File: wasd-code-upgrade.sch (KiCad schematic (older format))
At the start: 24 parts, among them J101 Conn_ARM_JTAG_SWD_10, J102 TC2030, J103 OLED, Q101 ZXTN08400BFF, Q102 ZXTP25020CFFTA, U101 STM32L422CBTx, U102 MIC5205-3.3YM5, U103 TC74VHC238F

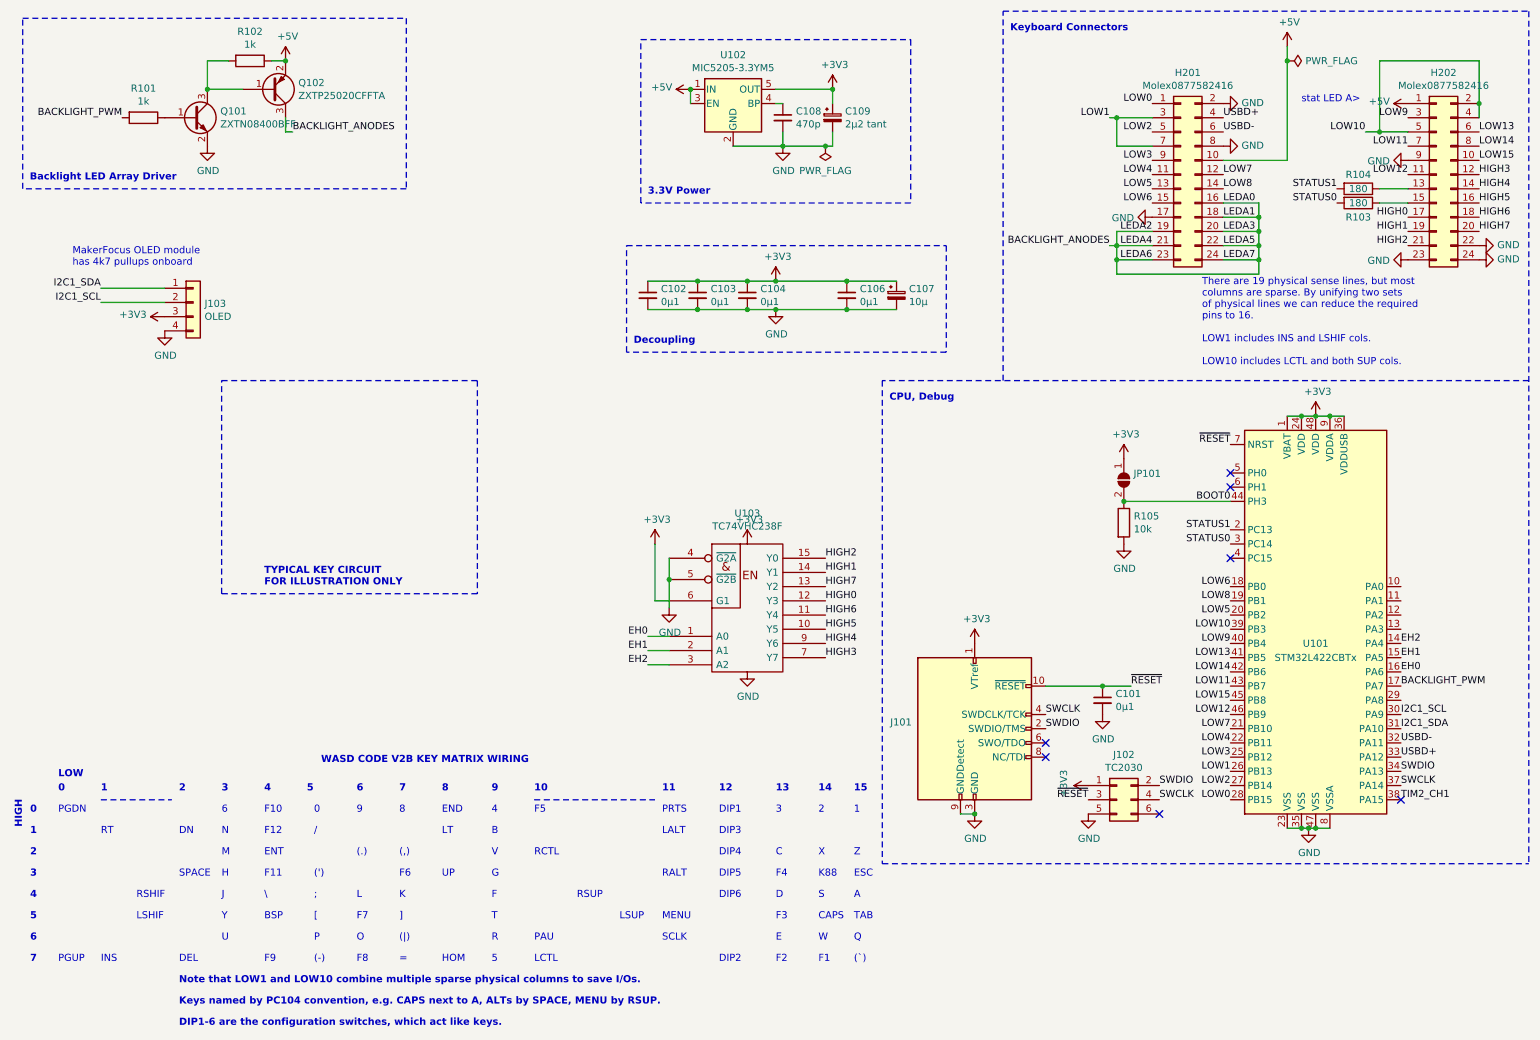
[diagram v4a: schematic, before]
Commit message: wasd-code-upgrade: tidy schematic
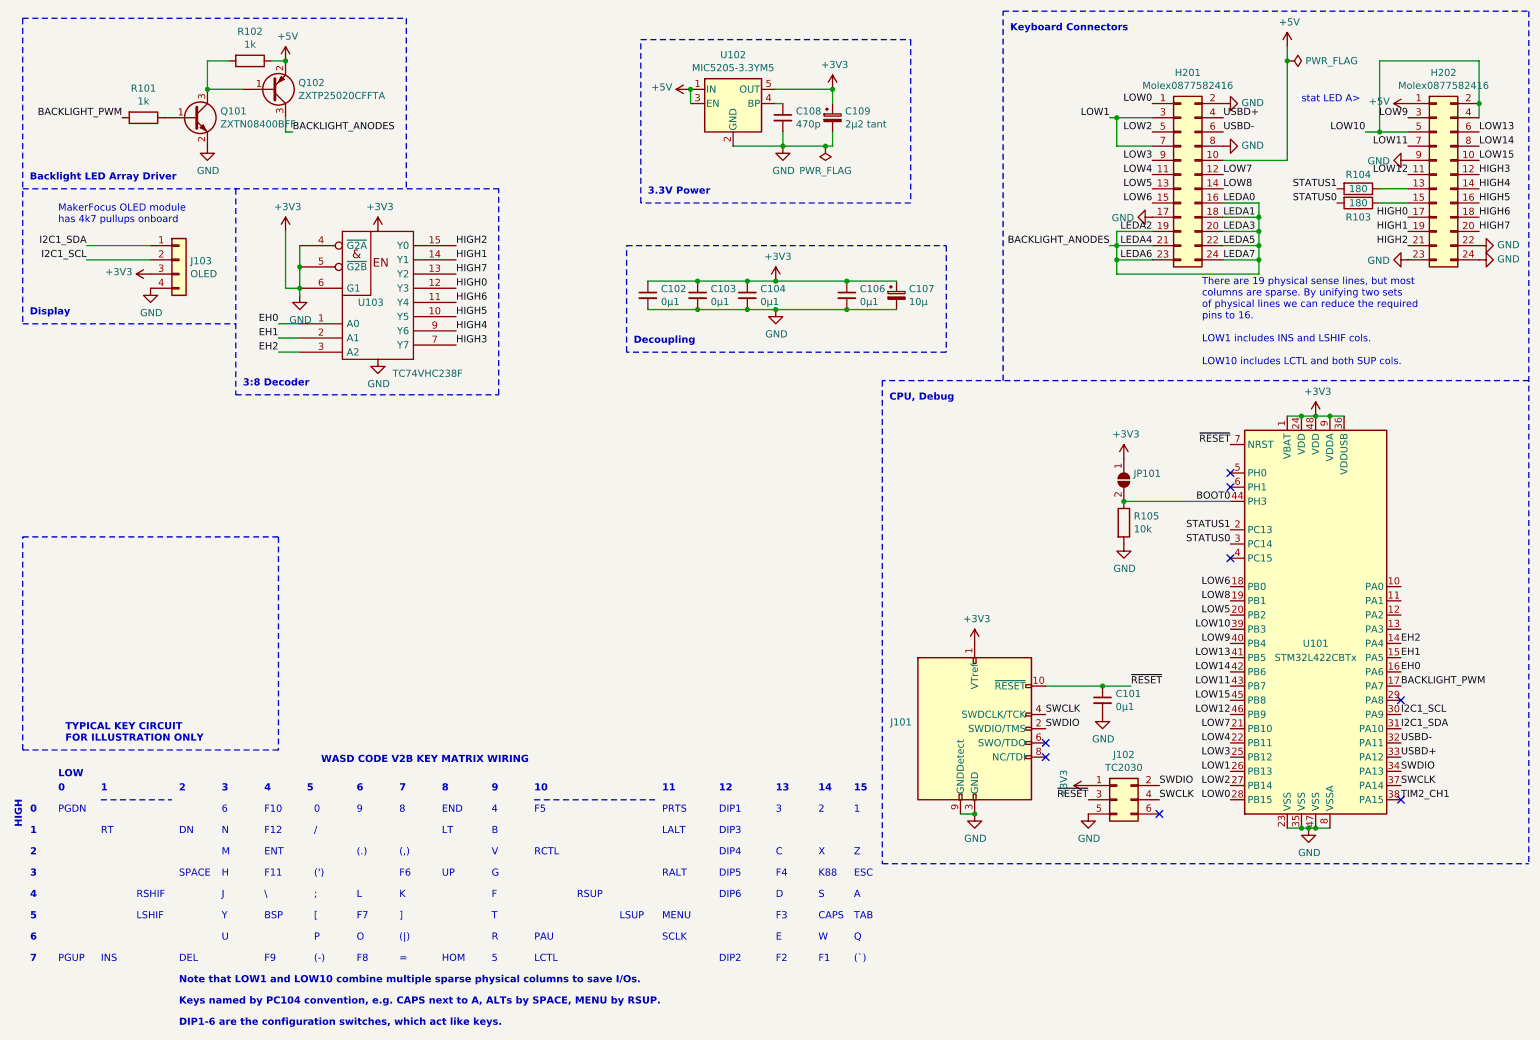
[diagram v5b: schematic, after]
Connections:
- net GND is gone; now on net +3V3: C101.2, C102.2, C103.2, C104.2, C106.2, C107.2, C108.2, C109.2, H201.17 (Pin_17), H201.2 (Pin_2), H201.8 (Pin_8), H202.22 (Pin_22), H202.23 (Pin_23), H202.24 (Pin_24), H202.9 (Pin_9), J101.3 (GND), J101.5 (GND), J101.9 (GNDDetect), J102.5 (Pin_5), J103.4 (Pin_4), Q101.2 (E), R105.2, U101.23 (VSS), U101.35 (VSS), U101.47 (VSS), U101.8 (VSSA), U102.2 (GND), U103.4 (~G2A), U103.5 (~G2B), U103.8 (GND)
- no-connect marks 7 -> 8
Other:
- note added: "3:8 Decoder"
- note added: "Display"
- moved on the sheet: J103, U103
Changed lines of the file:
@@
 Note that LOW1 and LOW10 combine multiple sparse physical columns to save I/Os.
 $Bitmap
-Pos 2900 3750
+Pos 1500 4850
 Scale 1.000000
 Data
@@
 EndData
 $EndBitmap
-Text Notes 2300 4550 0    50   ~ 10
+Text Notes 900  5650 0    50   ~ 10
 TYPICAL KEY CIRCUIT\nFOR ILLUSTRATION ONLY
 Wire Notes Line
-	2000 3100 3800 3100
-Wire Notes Line
-	3800 3100 3800 4600
-Wire Notes Line
-	3800 4600 2000 4600
-Wire Notes Line
-	2000 4600 2000 3100
+	600  4200 2400 4200
+Wire Notes Line
+	2400 4200 2400 5700
+Wire Notes Line
+	2400 5700 600  5700
+Wire Notes Line
+	600  5700 600  4200
 Text Notes 2700 5800 0    50   ~ 10
 WASD CODE V2B KEY MATRIX WIRING
@@
 Wire Notes Line
 	3300 550  3300 1750
-Wire Notes Line
-	3300 1750 600  1750
-Wire Notes Line
-	600  1750 600  550
 Wire Notes Line
 	600  550  3300 550
@@
 L power:+3V3 #PWR0126
 U 1 1 5F3B29C9
-P 5700 4250
-F 0 "#PWR0126" H 5700 4100 50  0001 C CNN
-F 1 "+3V3" H 5715 4423 50  0000 C CNN
-F 2 "" H 5700 4250 50  0001 C CNN
-F 3 "" H 5700 4250 50  0001 C CNN
-	1    5700 4250
+P 3100 2050
+F 0 "#PWR0126" H 3100 1900 50  0001 C CNN
+F 1 "+3V3" H 3115 2223 50  0000 C CNN
+F 2 "" H 3100 2050 50  0001 C CNN
+F 3 "" H 3100 2050 50  0001 C CNN
+	1    3100 2050
 	1    0    0    -1
 $EndComp
@@
 L power:GND #PWR0127
 U 1 1 5F3B302B
-P 5700 5150
-F 0 "#PWR0127" H 5700 4900 50  0001 C CNN
-F 1 "GND" H 5705 4977 50  0000 C CNN
-F 2 "" H 5700 5150 50  0001 C CNN
-F 3 "" H 5700 5150 50  0001 C CNN
-	1    5700 5150
-	1    0    0    -1
-$EndComp
-Wire Wire Line
-	5150 4650 5050 4650
-Wire Wire Line
-	5050 4650 5050 4250
+P 3100 2950
+F 0 "#PWR0127" H 3100 2700 50  0001 C CNN
+F 1 "GND" H 3105 2777 50  0000 C CNN
+F 2 "" H 3100 2950 50  0001 C CNN
+F 3 "" H 3100 2950 50  0001 C CNN
+	1    3100 2950
+	1    0    0    -1
+$EndComp
+Wire Wire Line
+	2550 2450 2450 2450
+Wire Wire Line
+	2450 2450 2450 2050
 $Comp
 L power:+3V3 #PWR0128
 U 1 1 5F3B62DA
-P 5050 4250
-F 0 "#PWR0128" H 5050 4100 50  0001 C CNN
-F 1 "+3V3" H 5065 4423 50  0000 C CNN
-F 2 "" H 5050 4250 50  0001 C CNN
-F 3 "" H 5050 4250 50  0001 C CNN
-	1    5050 4250
+P 2450 2050
+F 0 "#PWR0128" H 2450 1900 50  0001 C CNN
+F 1 "+3V3" H 2465 2223 50  0000 C CNN
+F 2 "" H 2450 2050 50  0001 C CNN
+F 3 "" H 2450 2050 50  0001 C CNN
+	1    2450 2050
 	1    0    0    -1
 $EndComp
@@
 L 74xx_IEEE:74HC238 U103
 U 1 1 5F3A148E
-P 5700 4550
-F 0 "U103" H 5700 5066 50  0000 C CNN
-F 1 "TC74VHC238F" H 5700 4975 50  0000 C CNN
-F 2 "vssop:VSSOP-16_3.0x4.25mm_P0.5mm" H 5700 4550 50  0001 C CNN
-F 3 "" H 5700 4550 50  0001 C CNN
-	1    5700 4550
-	1    0    0    -1
-$EndComp
-Wire Wire Line
-	5150 4350 5150 4500
-Connection ~ 5150 4500
+P 3100 2350
+F 0 "U103" H 3050 2150 50  0000 C CNN
+F 1 "TC74VHC238F" H 3450 1650 50  0000 C CNN
+F 2 "vssop:VSSOP-16_3.0x4.25mm_P0.5mm" H 3100 2350 50  0001 C CNN
+F 3 "" H 3100 2350 50  0001 C CNN
+	1    3100 2350
+	1    0    0    -1
+$EndComp
+Wire Wire Line
+	2550 2150 2550 2300
+Connection ~ 2550 2300
 $Comp
 L power:GND #PWR0129
 U 1 1 5F3BB24A
-P 5150 4700
-F 0 "#PWR0129" H 5150 4450 50  0001 C CNN
-F 1 "GND" H 5155 4527 50  0000 C CNN
-F 2 "" H 5150 4700 50  0001 C CNN
-F 3 "" H 5150 4700 50  0001 C CNN
-	1    5150 4700
-	1    0    0    -1
-$EndComp
-Wire Wire Line
-	5150 4900 5000 4900
-Wire Wire Line
-	5150 5000 5000 5000
-Wire Wire Line
-	5150 5100 5000 5100
-Text Label 5000 4900 2    50   ~ 0
+P 2550 2500
+F 0 "#PWR0129" H 2550 2250 50  0001 C CNN
+F 1 "GND" H 2555 2327 50  0000 C CNN
+F 2 "" H 2550 2500 50  0001 C CNN
+F 3 "" H 2550 2500 50  0001 C CNN
+	1    2550 2500
+	1    0    0    -1
+$EndComp
+Wire Wire Line
+	2550 2700 2400 2700
+Wire Wire Line
+	2550 2800 2400 2800
+Wire Wire Line
+	2550 2900 2400 2900
+Text Label 2400 2700 2    50   ~ 0
 EH0
-Text Label 5000 5000 2    50   ~ 0
+Text Label 2400 2800 2    50   ~ 0
 EH1
-Text Label 5000 5100 2    50   ~ 0
+Text Label 2400 2900 2    50   ~ 0
 EH2
-Text Label 6250 5050 0    50   ~ 0
+Text Label 3650 2850 0    50   ~ 0
 HIGH3
-Text Label 6250 4950 0    50   ~ 0
+Text Label 3650 2750 0    50   ~ 0
 HIGH4
-Text Label 6250 4850 0    50   ~ 0
+Text Label 3650 2650 0    50   ~ 0
 HIGH5
-Text Label 6250 4750 0    50   ~ 0
+Text Label 3650 2550 0    50   ~ 0
 HIGH6
-Text Label 6250 4650 0    50   ~ 0
+Text Label 3650 2450 0    50   ~ 0
 HIGH0
-Text Label 6250 4550 0    50   ~ 0
+Text Label 3650 2350 0    50   ~ 0
 HIGH7
-Text Label 6250 4450 0    50   ~ 0
+Text Label 3650 2250 0    50   ~ 0
 HIGH1
-Text Label 6250 4350 0    50   ~ 0
+Text Label 3650 2150 0    50   ~ 0
 HIGH2
 Wire Wire Line
-	5150 4500 5150 4700
+	2550 2300 2550 2450
 Text Label 10300 5150 0    50   ~ 0
 EH0
@@
 L Connector_Generic:Conn_01x04 J103
 U 1 1 5F3EFF40
-P 1800 2550
-F 0 "J103" H 1880 2542 50  0000 L CNN
-F 1 "OLED" H 1880 2451 50  0000 L CNN
-F 2 "Connector_PinSocket_2.54mm:PinSocket_1x04_P2.54mm_Vertical_SMD_Pin1Left" H 1800 2550 50  0001 C CNN
-F 3 "~" H 1800 2550 50  0001 C CNN
-	1    1800 2550
+P 1700 2250
+F 0 "J103" H 1780 2242 50  0000 L CNN
+F 1 "OLED" H 1780 2151 50  0000 L CNN
+F 2 "Connector_PinSocket_2.54mm:PinSocket_1x04_P2.54mm_Vertical_SMD_Pin1Left" H 1700 2250 50  0001 C CNN
+F 3 "~" H 1700 2250 50  0001 C CNN
+	1    1700 2250
 	1    0    0    -1
 $EndComp
@@
 L power:GND #PWR0130
 U 1 1 5F3F060A
-P 1600 2750
-F 0 "#PWR0130" H 1600 2500 50  0001 C CNN
-F 1 "GND" H 1605 2577 50  0000 C CNN
-F 2 "" H 1600 2750 50  0001 C CNN
-F 3 "" H 1600 2750 50  0001 C CNN
-	1    1600 2750
+P 1500 2450
+F 0 "#PWR0130" H 1500 2200 50  0001 C CNN
+F 1 "GND" H 1505 2277 50  0000 C CNN
+F 2 "" H 1500 2450 50  0001 C CNN
+F 3 "" H 1500 2450 50  0001 C CNN
+	1    1500 2450
 	1    0    0    -1
 $EndComp
@@
 L power:+3V3 #PWR0131
 U 1 1 5F3F136D
-P 1600 2650
-F 0 "#PWR0131" H 1600 2500 50  0001 C CNN
-F 1 "+3V3" V 1615 2778 50  0000 L CNN
-F 2 "" H 1600 2650 50  0001 C CNN
-F 3 "" H 1600 2650 50  0001 C CNN
-	1    1600 2650
+P 1500 2350
+F 0 "#PWR0131" H 1500 2200 50  0001 C CNN
+F 1 "+3V3" V 1515 2478 50  0000 L CNN
+F 2 "" H 1500 2350 50  0001 C CNN
+F 3 "" H 1500 2350 50  0001 C CNN
+	1    1500 2350
 	0    -1   -1   0
 $EndComp
 Wire Wire Line
-	1600 2450 1150 2450
-Text Label 1150 2450 2    50   ~ 0
+	1500 2150 1050 2150
+Text Label 1050 2150 2    50   ~ 0
 I2C1_SDA
-Text Label 1150 2550 2    50   ~ 0
+Text Label 1050 2250 2    50   ~ 0
 I2C1_SCL
 Wire Wire Line
-	1150 2550 1600 2550
-Text Notes 950  2300 0    50   ~ 0
+	1050 2250 1500 2250
+Text Notes 850  2000 0    50   ~ 0
 MakerFocus OLED module\nhas 4k7 pullups onboard
+Wire Notes Line
+	600  2700 2100 2700
+Wire Notes Line
+	600  550  600  2700
+Text Notes 650  2650 0    50   ~ 10
+Display
+Connection ~ 2550 2450
+Wire Wire Line
+	2550 2450 2550 2500
+Wire Notes Line
+	2100 3200 3950 3200
+Wire Notes Line
+	3950 3200 3950 1750
+Wire Notes Line
+	600  1750 3950 1750
+Wire Notes Line
+	2100 1750 2100 3200
+Text Notes 2150 3150 0    50   ~ 10
+3:8 Decoder
+NoConn ~ 10300 5350
 $EndSCHEMATC

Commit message: wasd-code-upgrade: rework after playing with v1
- Move _very bright_ status LEDs to PWM-capable pins.
- Fix mistakes in matrix.
- Simplify some layout to move more things to topside.
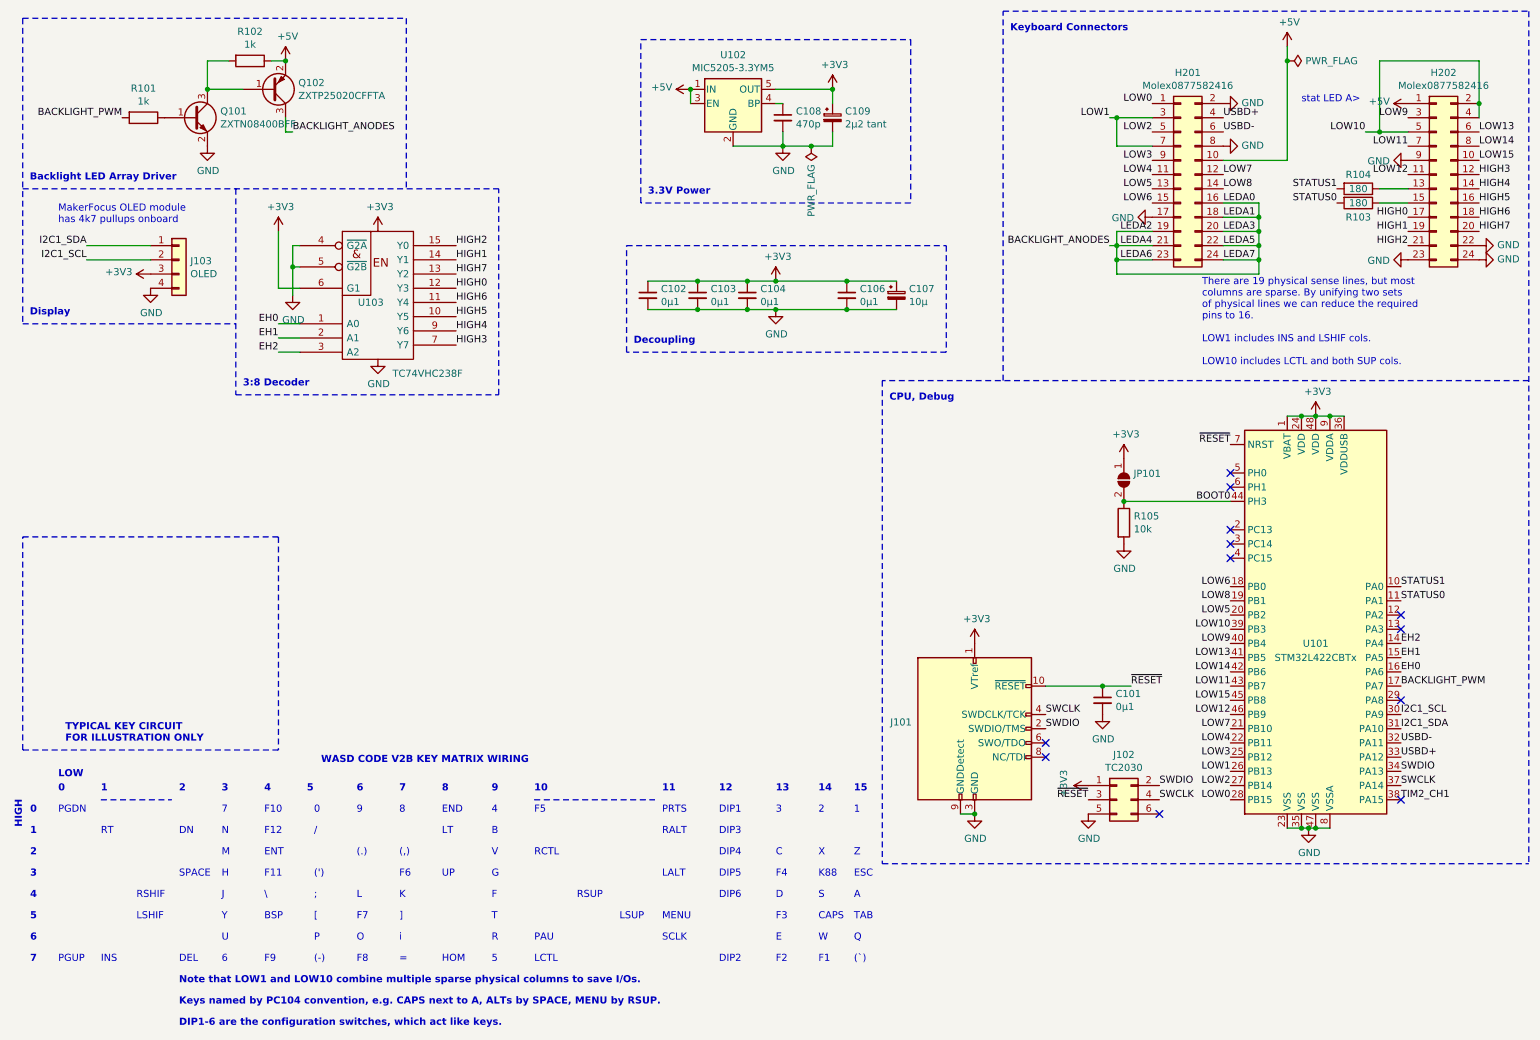
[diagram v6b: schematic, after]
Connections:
- net +3V3: no longer C101.2, C102.2, C103.2, C104.2, C106.2, C107.2, C108.2, C109.2, H201.17 (Pin_17), H201.2 (Pin_2), H201.8 (Pin_8), H202.22 (Pin_22), H202.23 (Pin_23), H202.24 (Pin_24), H202.9 (Pin_9), J101.3 (GND), J101.5 (GND), J101.9 (GNDDetect), J102.5 (Pin_5), J103.4 (Pin_4), Q101.2 (E), R105.2, U101.23 (VSS), U101.35 (VSS), U101.47 (VSS), U101.8 (VSSA), U102.2 (GND), U103.4 (~G2A), U103.5 (~G2B), U103.8 (GND)
- net STATUS0: now also U101.11 (PA1); no longer U101.3 (PC14)
- net STATUS1: now also U101.10 (PA0); no longer U101.2 (PC13)
- new net GND: C101.2, C102.2, C103.2, C104.2, C106.2, C107.2, C108.2, C109.2, H201.17 (Pin_17), H201.2 (Pin_2), H201.8 (Pin_8), H202.22 (Pin_22), H202.23 (Pin_23), H202.24 (Pin_24), H202.9 (Pin_9), J101.3 (GND), J101.5 (GND), J101.9 (GNDDetect), J102.5 (Pin_5), J103.4 (Pin_4), Q101.2 (E), R105.2, U101.23 (VSS), U101.35 (VSS), U101.47 (VSS), U101.8 (VSSA), U102.2 (GND), U103.4 (~G2A), U103.5 (~G2B), U103.8 (GND)
- no-connect marks 8 -> 12
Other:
- note added: "i"
- note removed: "(|)"
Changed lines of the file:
@@
 Wire Wire Line
 	6300 1350 6300 1450
-Wire Wire Line
-	6300 1450 6250 1450
 Connection ~ 5950 1450
 $Comp
@@
 Wire Wire Line
 	5900 1050 6300 1050
-$Comp
-L power:PWR_FLAG #FLG0101
-U 1 1 5F4C4858
-P 6250 1450
-F 0 "#FLG0101" H 6250 1525 50  0001 C CNN
-F 1 "PWR_FLAG" H 6250 1623 50  0000 C CNN
-F 2 "" H 6250 1450 50  0001 C CNN
-F 3 "~" H 6250 1450 50  0001 C CNN
-	1    6250 1450
-	-1   0    0    1
-$EndComp
-Connection ~ 6250 1450
-Wire Wire Line
-	5950 1450 6250 1450
 Wire Wire Line
 	9050 1850 9300 1850
@@
 Wire Wire Line
 	9300 1950 9300 2050
-Text Label 9100 4150 2    50   ~ 0
+Text Label 10300 4550 0    50   ~ 0
 STATUS1
-Text Label 9100 4250 2    50   ~ 0
+Text Label 10300 4650 0    50   ~ 0
 STATUS0
 Text Label 10300 5250 0    50   ~ 0
@@
 DEL
 Text Notes 2000 6150 0    50   ~ 0
-6
+7
 Text Notes 2000 6300 0    50   ~ 0
 N
@@
 ]
 Text Notes 3250 7050 0    50   ~ 0
-(|)
+i
 Text Notes 3250 7200 0    50   ~ 0
 =
@@
 PRTS
 Text Notes 5100 6300 0    50   ~ 0
+RALT
+Text Notes 5100 6600 0    50   ~ 0
 LALT
-Text Notes 5100 6600 0    50   ~ 0
-RALT
 Text Notes 5100 6900 0    50   ~ 0
 MENU
@@
 $EndComp
 Wire Wire Line
-	2550 2450 2450 2450
-Wire Wire Line
-	2450 2450 2450 2050
+	2550 2450 2400 2450
+Wire Wire Line
+	2400 2450 2400 2050
 $Comp
 L power:+3V3 #PWR0128
 U 1 1 5F3B62DA
-P 2450 2050
-F 0 "#PWR0128" H 2450 1900 50  0001 C CNN
-F 1 "+3V3" H 2465 2223 50  0000 C CNN
-F 2 "" H 2450 2050 50  0001 C CNN
-F 3 "" H 2450 2050 50  0001 C CNN
-	1    2450 2050
+P 2400 2050
+F 0 "#PWR0128" H 2400 1900 50  0001 C CNN
+F 1 "+3V3" H 2415 2223 50  0000 C CNN
+F 2 "" H 2400 2050 50  0001 C CNN
+F 3 "" H 2400 2050 50  0001 C CNN
+	1    2400 2050
 	1    0    0    -1
 $EndComp
@@
 	1    0    0    -1
 $EndComp
-Wire Wire Line
-	2550 2150 2550 2300
-Connection ~ 2550 2300
 $Comp
 L power:GND #PWR0129
 U 1 1 5F3BB24A
-P 2550 2500
-F 0 "#PWR0129" H 2550 2250 50  0001 C CNN
-F 1 "GND" H 2555 2327 50  0000 C CNN
-F 2 "" H 2550 2500 50  0001 C CNN
-F 3 "" H 2550 2500 50  0001 C CNN
-	1    2550 2500
+P 2500 2500
+F 0 "#PWR0129" H 2500 2250 50  0001 C CNN
+F 1 "GND" H 2505 2327 50  0000 C CNN
+F 2 "" H 2500 2500 50  0001 C CNN
+F 3 "" H 2500 2500 50  0001 C CNN
+	1    2500 2500
 	1    0    0    -1
 $EndComp
@@
 Text Label 3650 2150 0    50   ~ 0
 HIGH2
-Wire Wire Line
-	2550 2300 2550 2450
 Text Label 10300 5150 0    50   ~ 0
 EH0
@@
 Text Notes 650  2650 0    50   ~ 10
 Display
-Connection ~ 2550 2450
-Wire Wire Line
-	2550 2450 2550 2500
 Wire Notes Line
 	2100 3200 3950 3200
@@
 3:8 Decoder
 NoConn ~ 10300 5350
+Wire Wire Line
+	5950 1450 6150 1450
+Wire Wire Line
+	2550 2150 2500 2150
+Wire Wire Line
+	2500 2150 2500 2300
+Wire Wire Line
+	2550 2300 2500 2300
+Connection ~ 2500 2300
+Wire Wire Line
+	2500 2300 2500 2500
+NoConn ~ 10300 4750
+NoConn ~ 10300 4850
+NoConn ~ 9100 4250
+NoConn ~ 9100 4150
+$Comp
+L power:PWR_FLAG #FLG0101
+U 1 1 5F423B07
+P 6150 1450
+F 0 "#FLG0101" H 6150 1525 50  0001 C CNN
+F 1 "PWR_FLAG" V 6150 1578 50  0000 L CNN
+F 2 "" H 6150 1450 50  0001 C CNN
+F 3 "~" H 6150 1450 50  0001 C CNN
+	1    6150 1450
+	-1   0    0    1
+$EndComp
+Connection ~ 6150 1450
+Wire Wire Line
+	6150 1450 6300 1450
+Text Notes 2000 7200 0    50   ~ 0
+6
 $EndSCHEMATC
